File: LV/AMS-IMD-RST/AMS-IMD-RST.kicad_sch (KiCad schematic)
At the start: 53 parts, among them J1 2P Droit 2-11-2022, J2 2P Droit 2-11-2022, J3 2P Droit 2-11-2022, J4 2P Droit 2-11-2022, J5 2P Droit 2-11-2022, J7 4P Droit 22-11-2042, K1 Relais PCB, K2 Bistable V23079B1201B301, K3 Relais PCB, K4 Bistable V23079B1201B301, Q1 NMOS SQ2348ES-T1_GE3, Q2 NMOS SQ2348ES-T1_GE3, Q3 NMOS SQ2348ES-T1_GE3, Q4 NMOS SQ2348ES-T1_GE3, Q5 NMOS SQ2348ES-T1_GE3, Q6 NMOS SQ2348ES-T1_GE3, U1 Alim LP TSR_0.5-2450, U2 ${SIM.PARAMS}, U3 LM358, U4 LM397, U5 LM397, U6 LM358

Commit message: SCS added
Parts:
- removed C3, C6: 1u, EPSA_lib:CAPC2012X130N, symbol EPSA_Lib:Condensateur 0805Y1000104JXT
- removed DU2: Opamp_Dual, Package_SO:TSSOP-8_4.4x3mm_P0.65mm, symbol EPSA_Lib:Comparator_Dual
- removed R1: 500k, EPSA_lib:RESC3216X70N, symbol EPSA_Lib:Résistance RK73H2BLTDD2152F
- removed R10, R7: 82k, EPSA_lib:RESC3216X70N, symbol EPSA_Lib:Résistance RK73H2BLTDD2152F
- removed R2: 10k, symbol Device:R
- removed R4: 10k, EPSA_lib:RESC3216X70N, symbol EPSA_Lib:Résistance RK73H2BLTDD2152F
- removed R8, R9: 12k, EPSA_lib:RESC3216X70N, symbol EPSA_Lib:Résistance RK73H2BLTDD2152F
- removed U2: ${SIM.PARAMS}, Package_TO_SOT_SMD:SOT-353_SC-70-5_Handsoldering, symbol EPSA_Lib:Opamp
- removed U3, U6: LM358, symbol Amplifier_Operational:LM358
- removed U4, U5: LM397, Package_TO_SOT_SMD:SOT-23-5, symbol Comparator:LM397
- added R3, R7: 10k, symbol Device:R
- added R5, R6: 47k, symbol Device:R
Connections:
- net +5V: now also R3.1, R5.1
- net GND: now also R6.2, R7.2
- new net 1V: R5.2, R7.1
- new net 4V: R3.2, R6.1
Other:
- added sheet SCS_Input_Converter (${KIPRJMOD}/../scs_input_converter.kicad_sch)
- added sheet SCS_Input_Converter1 (${KIPRJMOD}/../scs_input_converter.kicad_sch)
- added sheet SCS_Input_Converter2 (${KIPRJMOD}/../scs_input_converter.kicad_sch)

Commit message: Finished V1.0 of Schematic and PCB
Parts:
- removed C2, C7, C8: 1u, EPSA_lib:CAPC2012X130N, symbol EPSA_Lib:Condensateur 0805Y1000104JXT
- removed D4, D5: LED, LED_THT:LED_D5.0mm, symbol Device:LED
- removed G1, G2: Gate NAND SN74AHCT1G00DBVR, EPSA_lib:SOT95P280X145-5N, symbol EPSA_Lib:Gate NAND SN74AHCT1G00DBVR
- removed G3: Gate AND SN74AHCT1G08DBVR, EPSA_lib:SOT95P280X145-5N, symbol EPSA_Lib:Gate AND SN74AHCT1G08DBVR
- removed K2, K4: Bistable V23079B1201B301, EPSA_lib:V23079B1201B301, symbol EPSA_Lib:Bistable V23079B1201B301
- removed Q1, Q2, Q3, Q4: NMOS SQ2348ES-T1_GE3, EPSA_lib:SOT95P237X112-3N, symbol EPSA_Lib:NMOS SQ2348ES-T1_GE3
- removed R11, R12: 500, EPSA_lib:RESC3216X70N, symbol EPSA_Lib:Résistance RK73H2BLTDD2152F
- removed R15: 3k9, EPSA_lib:RESC3216X70N, symbol EPSA_Lib:Résistance RK73H2BLTDD2152F
- removed R16, R17: 8k2, EPSA_lib:RESC3216X70N, symbol EPSA_Lib:Résistance RK73H2BLTDD2152F
- removed R18: 100k, EPSA_lib:RESC3216X70N, symbol EPSA_Lib:Résistance RK73H2BLTDD2152F
- added J6: 2P Droit 2-11-2022, EPSA_lib:MOLEX_22-11-2022, symbol EPSA_Lib:2P Droit 2-11-2022
- added R1: 4.3k, Resistor_SMD:R_0402_1005Metric, symbol Device:R
- added R2: 10k, Resistor_SMD:R_0402_1005Metric, symbol Device:R
- added U11: 74AUC2G00, Package_SO:SSOP-8_3.9x5.05mm_P1.27mm, symbol 74xGxx:74AUC2G00
- added U3: 74AHC1G32, Package_TO_SOT_SMD:SOT-23-5, symbol 74xGxx:74AHC1G32
- added U4: 74AUC2G04, Package_TO_SOT_SMD:SOT-23-6, symbol 74xGxx:74AUC2G04
- added U7: 74LS279, Package_SO:SOIC-16W_5.3x10.2mm_P1.27mm, symbol 74xx:74LS279
- C1: value C -> 10u
- D1, D2, D3: footprint LED_THT:LED_D5.0mm -> LED_THT:LED_D3.0mm
- R3, R6, R7: footprint (none) -> Resistor_SMD:R_0402_1005Metric
- R5: value 47k -> 4.3k; footprint (none) -> Resistor_SMD:R_0402_1005Metric
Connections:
- net +12V: now also C1.1; no longer C1.2
- net +5V: now also R1.1, U11.8 (VCC), U3.5 (VCC), U4.5 (VCC), U7.16 (VCC)
- net Button_Input_SCS: now also R1.2, R2.1
- net GND: now also C1.2, R2.2, U11.4 (GND), U3.3 (GND), U4.2 (GND), U7.8 (GND); no longer C1.1, J4.1, J5.1
- net Raw_AMS_OK: now also J5.1
- net Raw_IMD_OK: now also J4.1
- net SC_Closed_AMS: now also U4.3, U7.9 (Q)
- net SC_Closed_IMD: now also U4.1, U7.4 (Q)
- net AMS_State: now reaches D2.2 (A)
- net AMS_State: now also U11.2, U7.10 (~{R})
- net Button_Output_State: now reaches D3.2 (A)
- net Button_Output_State: now also U11.1, U11.5
- net IMD_State: now reaches D1.2 (A)
- net IMD_State: now also U11.6, U7.1 (~{R})
- net 1V renamed 3.5V
- net Button_Input renamed LED_Button
- net LED_Button: now also U3.4
- new net: U11.3, U7.2 (~{S}), U7.3 (~{S})
- new net: U11.7, U7.11 (~{S}), U7.12 (~{S})
- new net AMS_Led: J6.1, U3.2, U4.4
- new net IMD_Led: J6.2, U3.1, U4.6
- no-connect marks 0 -> 6
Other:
- sheet SCS_Input_Converter: file ${KIPRJMOD}/../scs_input_converter.kicad_sch -> ../scs_input_converter.kicad_sch
- sheet SCS_Input_Converter ports: added +3.5V; removed +1V
- sheet SCS_Input_Converter1: file ${KIPRJMOD}/../scs_input_converter.kicad_sch -> ../scs_input_converter.kicad_sch
- sheet SCS_Input_Converter1 ports: added +3.5V; removed +1V
- sheet SCS_Input_Converter2: file ${KIPRJMOD}/../scs_input_converter.kicad_sch -> ../scs_input_converter.kicad_sch
- sheet SCS_Input_Converter2 ports: added +3.5V; removed +1V
- note added: "Debug LED"
- moved on the sheet: C1

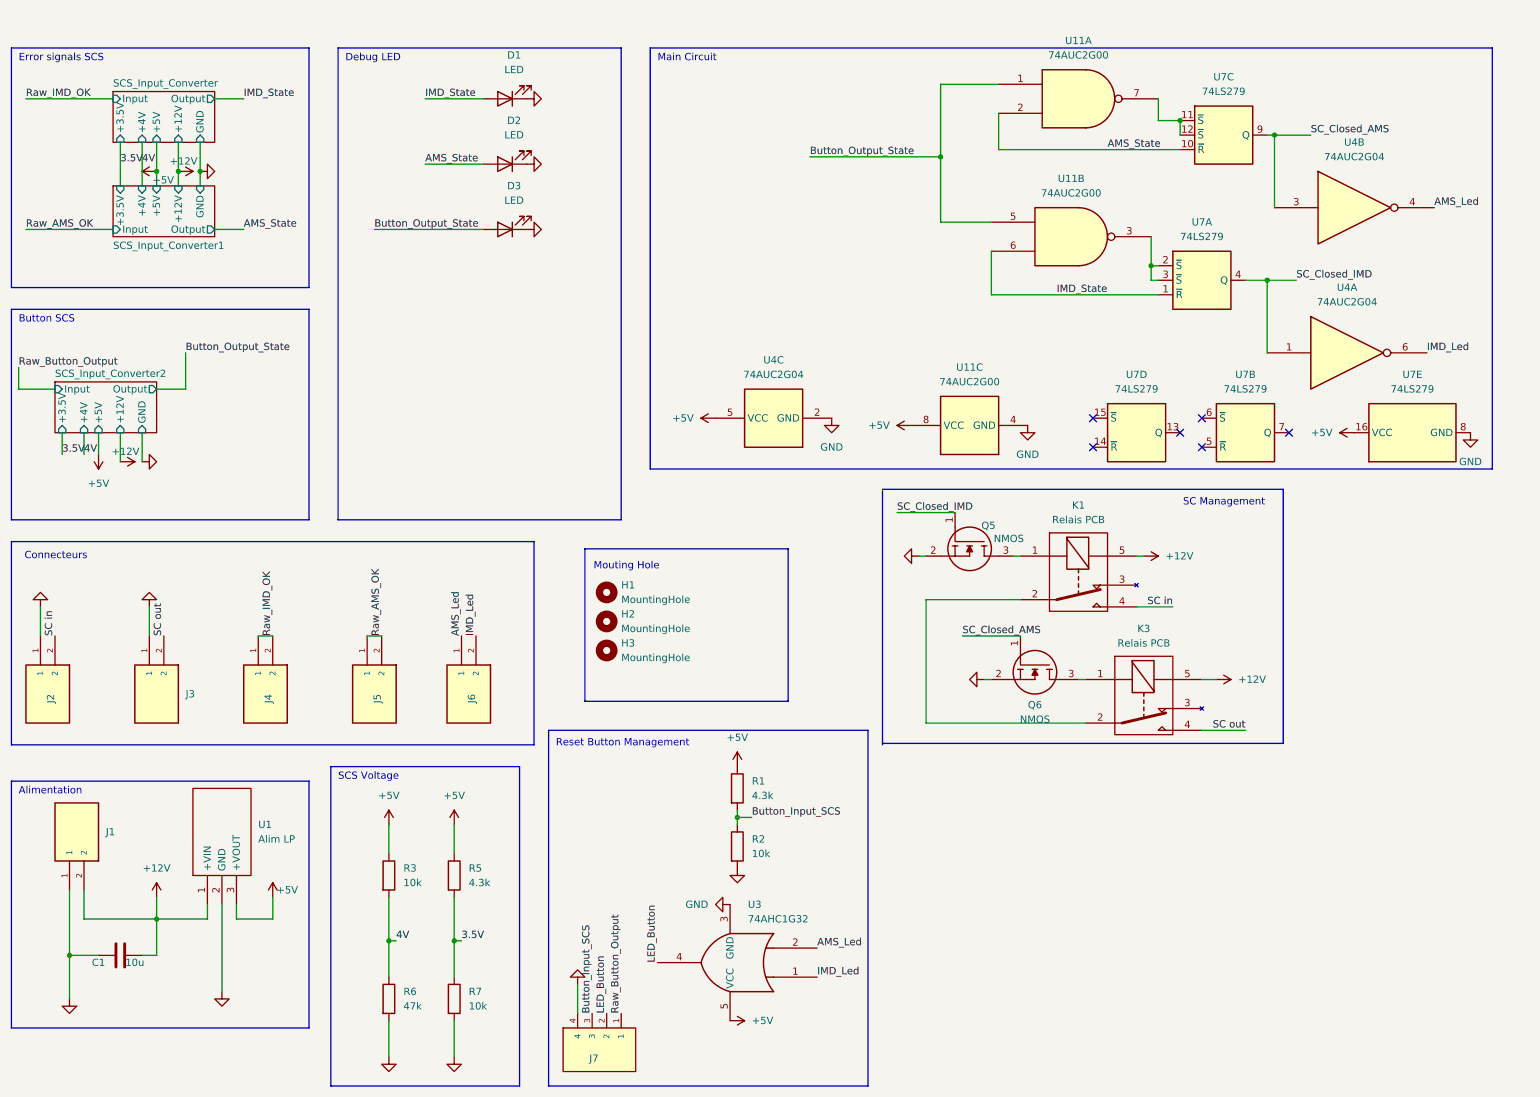
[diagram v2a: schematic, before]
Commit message: Added 2s lightning for T11.9.6 compliance
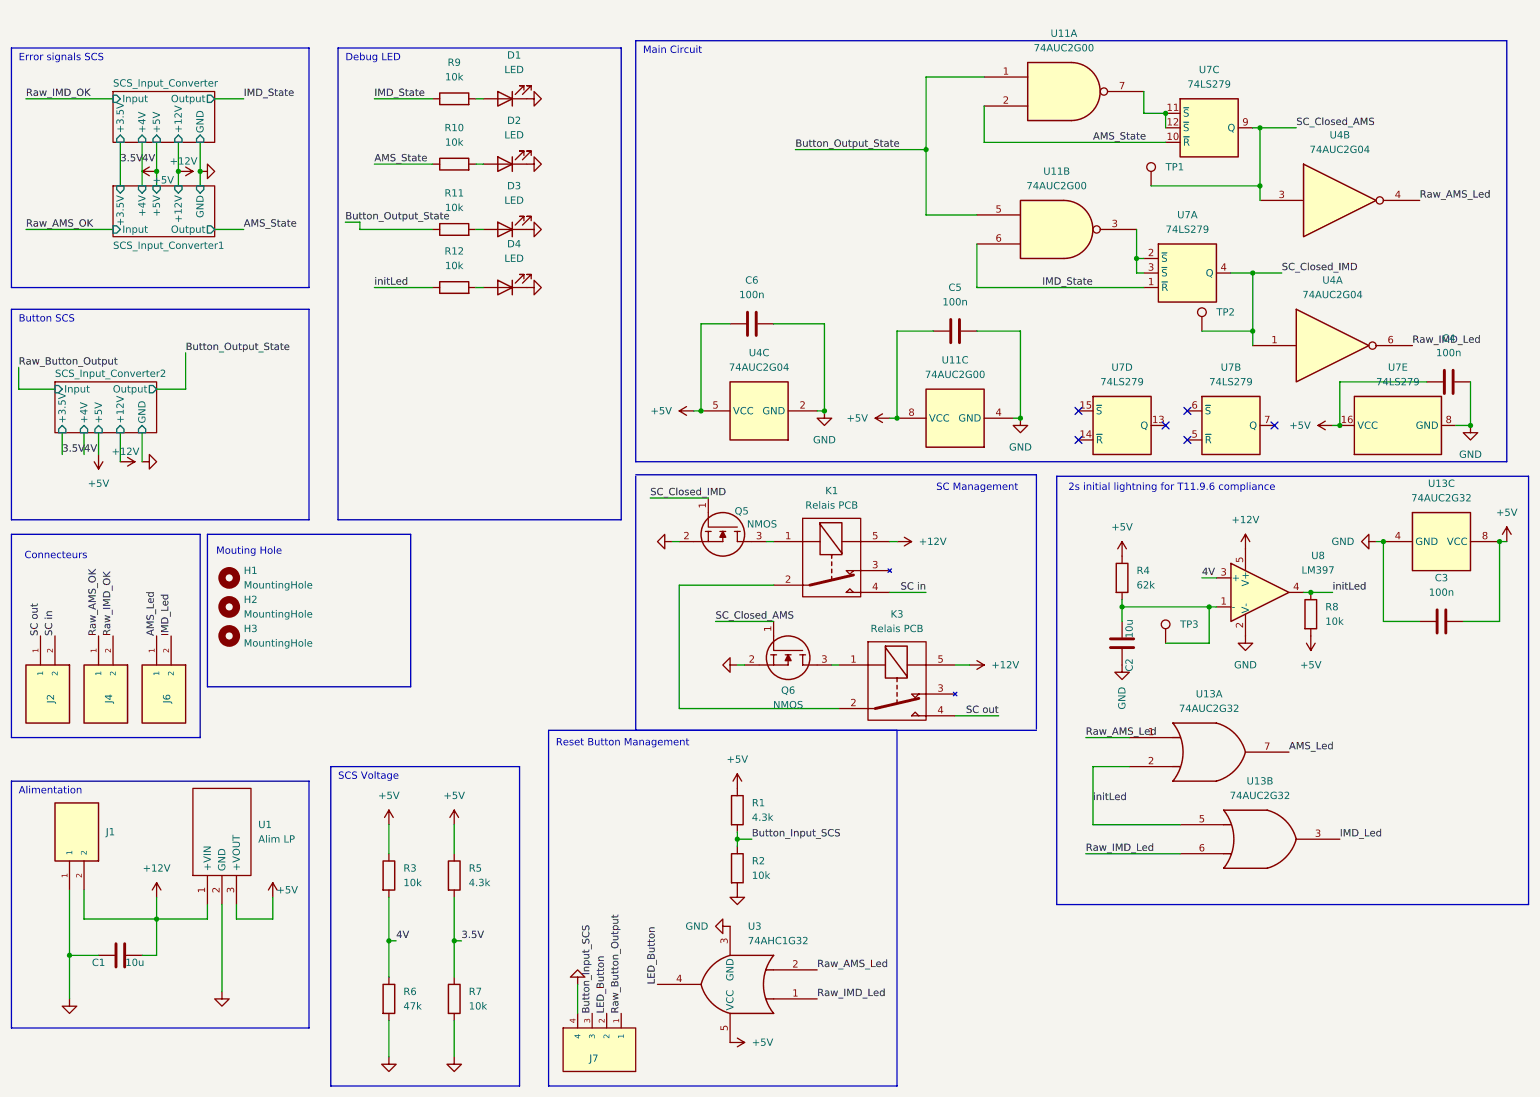
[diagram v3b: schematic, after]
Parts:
- removed J3, J5: 2P Droit 2-11-2022, EPSA_lib:MOLEX_22-11-2022, symbol EPSA_Lib:2P Droit 2-11-2022
- added C2: 10u, Capacitor_THT:CP_Radial_D5.0mm_P2.00mm, symbol Device:C
- added C3, C4, C5, C6: 100n, Capacitor_SMD:C_0805_2012Metric_Pad1.18x1.45mm_HandSolder, symbol Device:C
- added D4: LED, LED_THT:LED_D3.0mm, symbol Device:LED
- added R10, R11, R12, R8, R9: 10k, Resistor_SMD:R_0805_2012Metric_Pad1.20x1.40mm_HandSolder, symbol Device:R
- added R4: 62k, Resistor_SMD:R_0805_2012Metric_Pad1.20x1.40mm_HandSolder, symbol Device:R
- added TP1, TP2, TP3: ${SIM.PARAMS}, TestPoint:TestPoint_Pad_D1.0mm, symbol EPSA_lib:TestPoint
- added U13: 74AUC2G32, Package_SO:SSOP-8_3.9x5.05mm_P1.27mm, symbol 74xGxx:74AUC2G32
- added U8: LM397, Package_TO_SOT_SMD:SOT-23-5, symbol Comparator:LM397
- R1, R2, R3, R5, R6, R7: footprint Resistor_SMD:R_0402_1005Metric -> Resistor_SMD:R_0805_2012Metric_Pad1.20x1.40mm_HandSolder
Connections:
- net +12V: now also U8.5 (V+)
- net +5V: now also C3.2, C4.1, C5.1, C6.1, R4.1, R8.2, U13.8 (VCC)
- net 4V: now also U8.3 (+)
- net AMS_Led: now also U13.7; no longer U3.2, U4.4
- net AMS_State: now also R10.1; no longer D2.2 (A)
- net Button_Output_State: now also R11.1; no longer D3.2 (A)
- net GND: now also C2.2, C3.1, C4.2, C5.2, C6.2, D4.1 (K), U13.4 (GND), U8.2 (V-); no longer J2.1
- net IMD_Led: now also U13.3; no longer U3.1, U4.6
- net IMD_State: now also R9.1; no longer D1.2 (A)
- net Raw_AMS_OK: now also J4.1
- net Raw_IMD_OK: no longer J4.1
- net SC out: now also J2.1
- net SC_Closed_AMS: now also TP1.1
- net SC_Closed_IMD: now also TP2.1
- new net: D1.2 (A), R9.2
- new net: C2.1, R4.2, TP3.1, U8.1 (-)
- new net: D3.2 (A), R11.2
- new net: D4.2 (A), R12.2
- new net: D2.2 (A), R10.2
- new net Raw_AMS_Led: U13.1, U3.2, U4.4
- new net Raw_IMD_Led: U13.6, U3.1, U4.6
- new net initLed: R12.1, R8.1, U13.2, U13.5, U8.4
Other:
- note added: "2s initial lightning for T11.9.6 compliance"
- moved on the sheet: H1, H2, H3, J4, J6, K1, K3, Q5, Q6, R1, R2, U11A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
